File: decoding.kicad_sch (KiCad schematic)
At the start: 30 parts

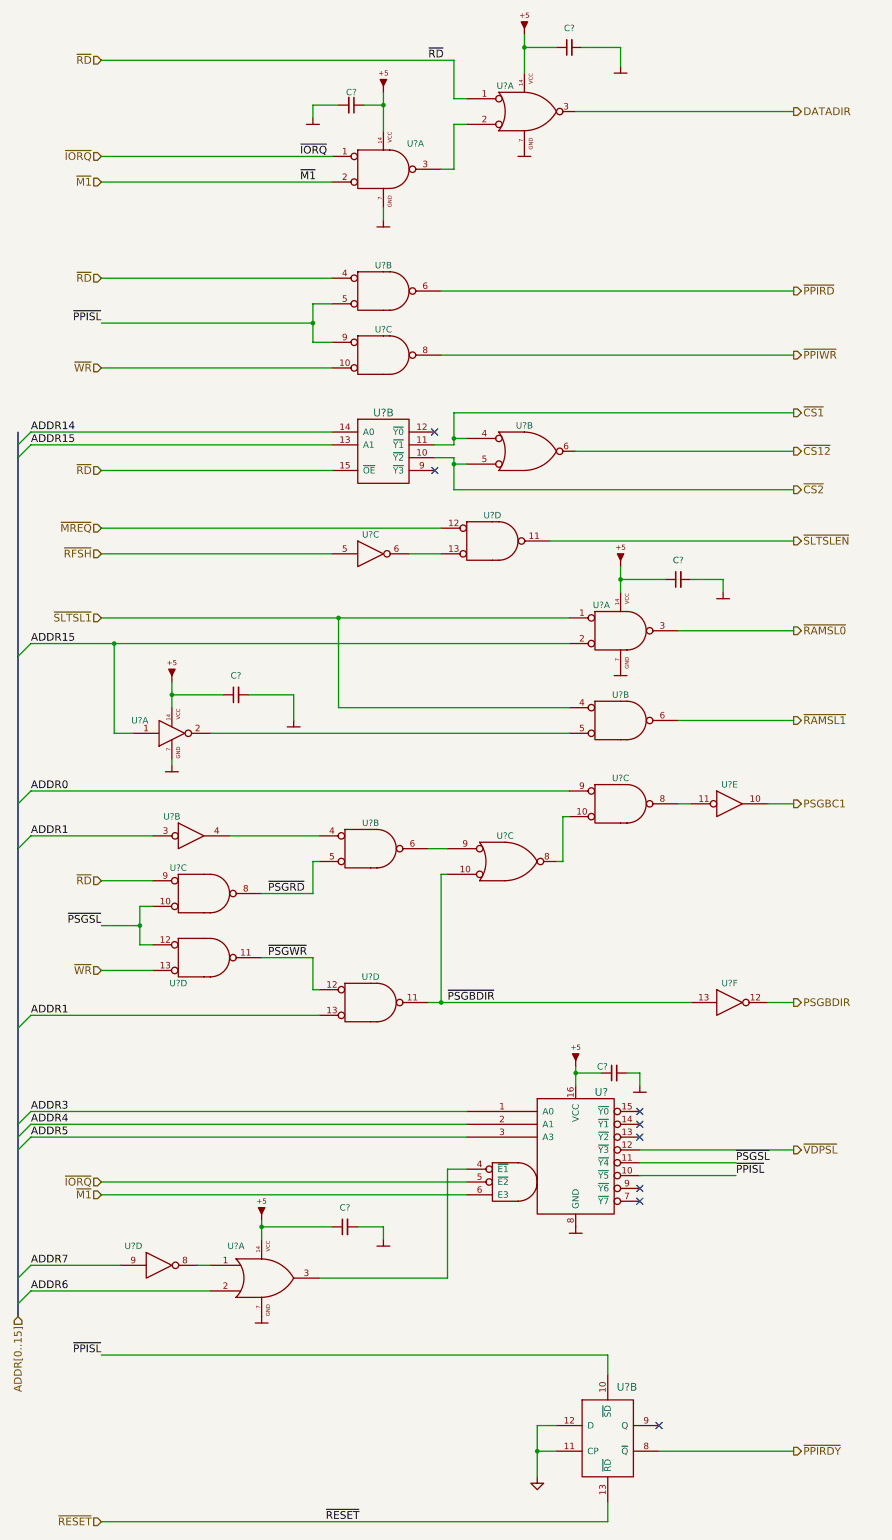
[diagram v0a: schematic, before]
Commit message: Fix wrong cap type in clock generator
Also fill some references automatically generated by KiCAD.
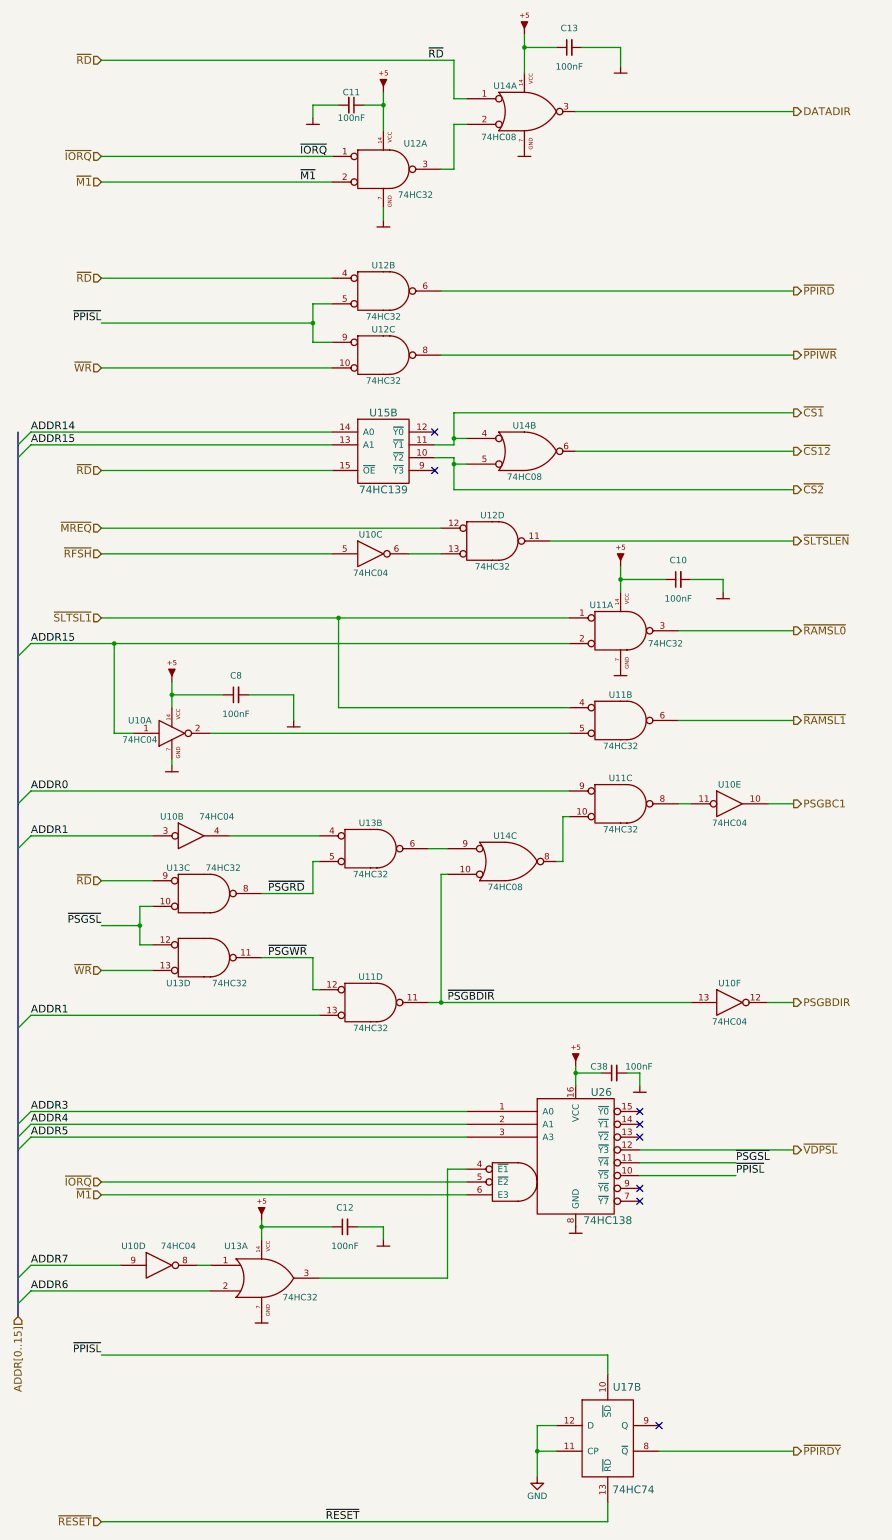
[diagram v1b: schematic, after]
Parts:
- C10, C11, C12, C13, C38, C8: renamed from C?; value (none) -> 100nF; footprint (none) -> artemisa:Disc_capacitor
- U10: renamed from U?; value (none) -> 74HC04; footprint (none) -> artemisa:DIP-14_300
- U11, U12, U13: renamed from U?; value (none) -> 74HC32; footprint (none) -> artemisa:DIP-14_300
- U14: renamed from U?; value (none) -> 74HC08; footprint (none) -> artemisa:DIP-14_300
- U15: renamed from U?; value (none) -> 74HC139; footprint (none) -> artemisa:DIP-16_300
- U17: renamed from U?; value (none) -> 74HC74; footprint (none) -> artemisa:DIP-14_300
- U26: renamed from U?; value (none) -> 74HC138; footprint (none) -> artemisa:DIP-16_300
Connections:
- net VCC: now also C10.1, C11.1, C12.1, C13.1, C38.1, C8.1, U10.14 (VCC), U11.14 (VCC), U12.14 (VCC), U13.14 (VCC), U14.14 (VCC), U26.16 (VCC)

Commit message: Upgrade project files to KiCad v8
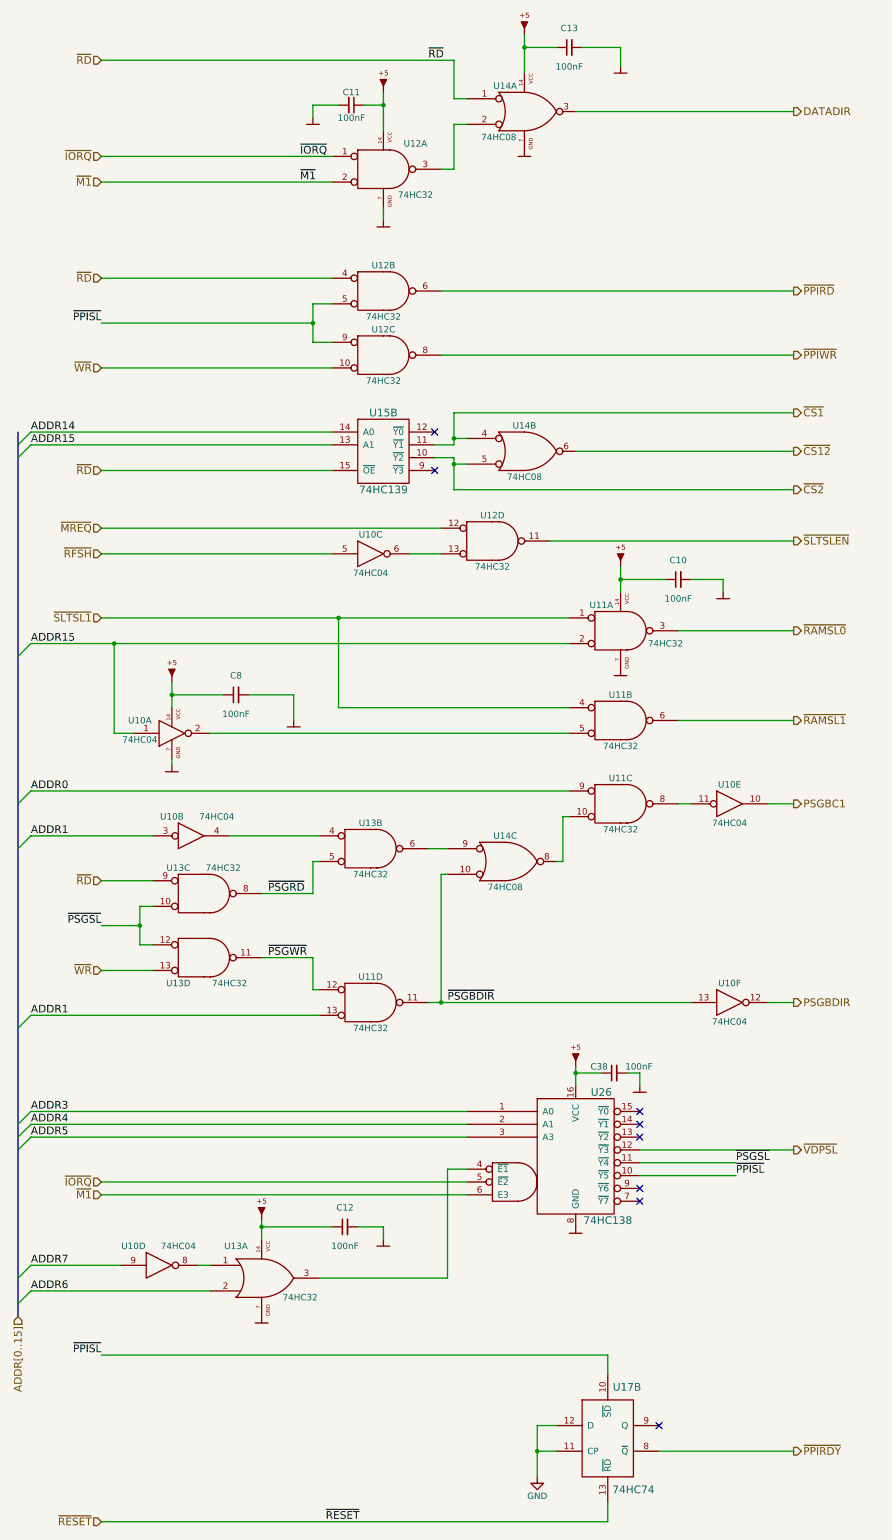
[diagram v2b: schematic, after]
